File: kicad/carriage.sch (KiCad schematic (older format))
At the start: 44 parts, among them CON10 Stepstick_Left_Connector, CON11 Stepstick_Right_Connector, CON12 Stepstick_Left_Connector, CON13 Stepstick_Right_Connector, CON14 Stepstick_Left_Connector, CON15 Stepstick_Right_Connector, CON9 Carriage, Q1 IRLR2905ZPBF, Q2 IRLR2905ZPBF, Q3 FDC6401N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

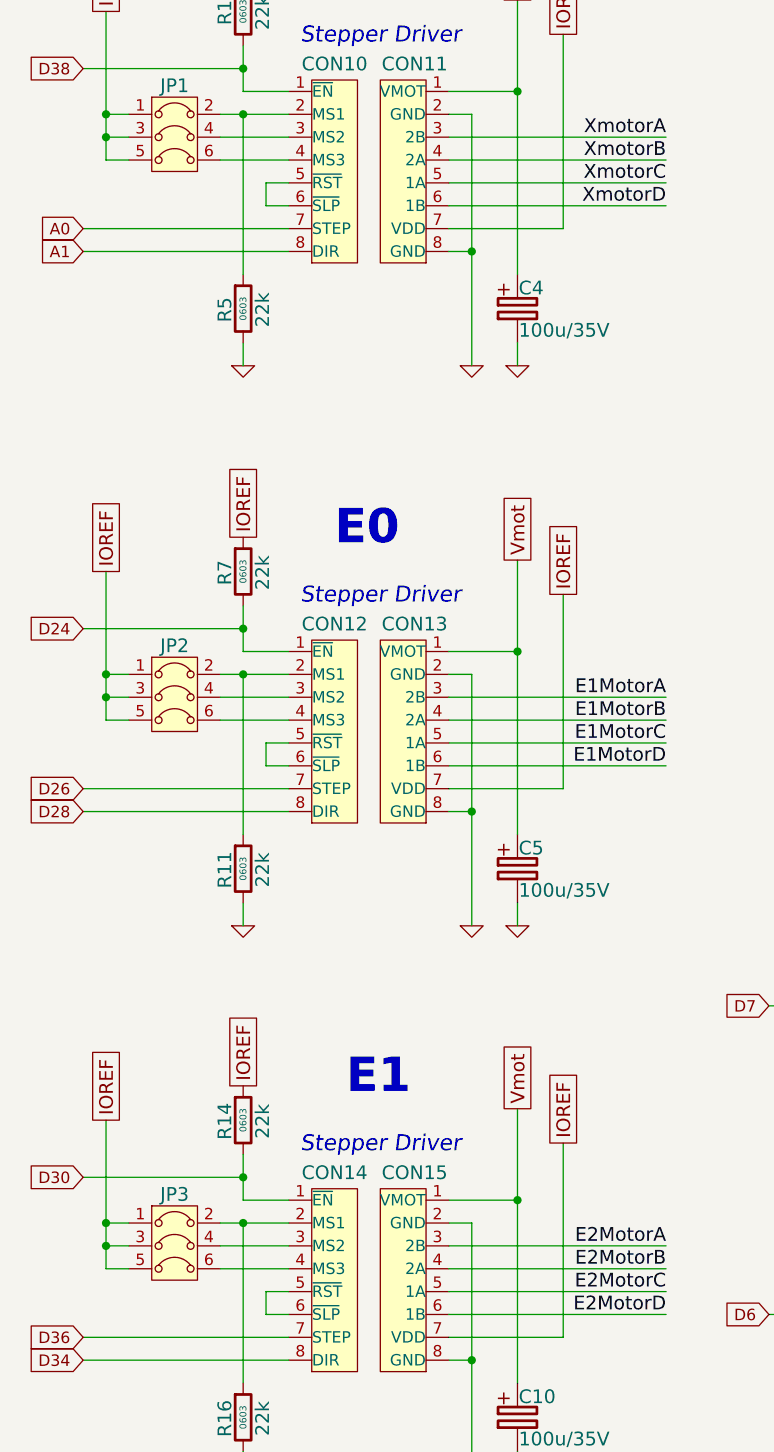
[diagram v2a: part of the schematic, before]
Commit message: Add footprint informations
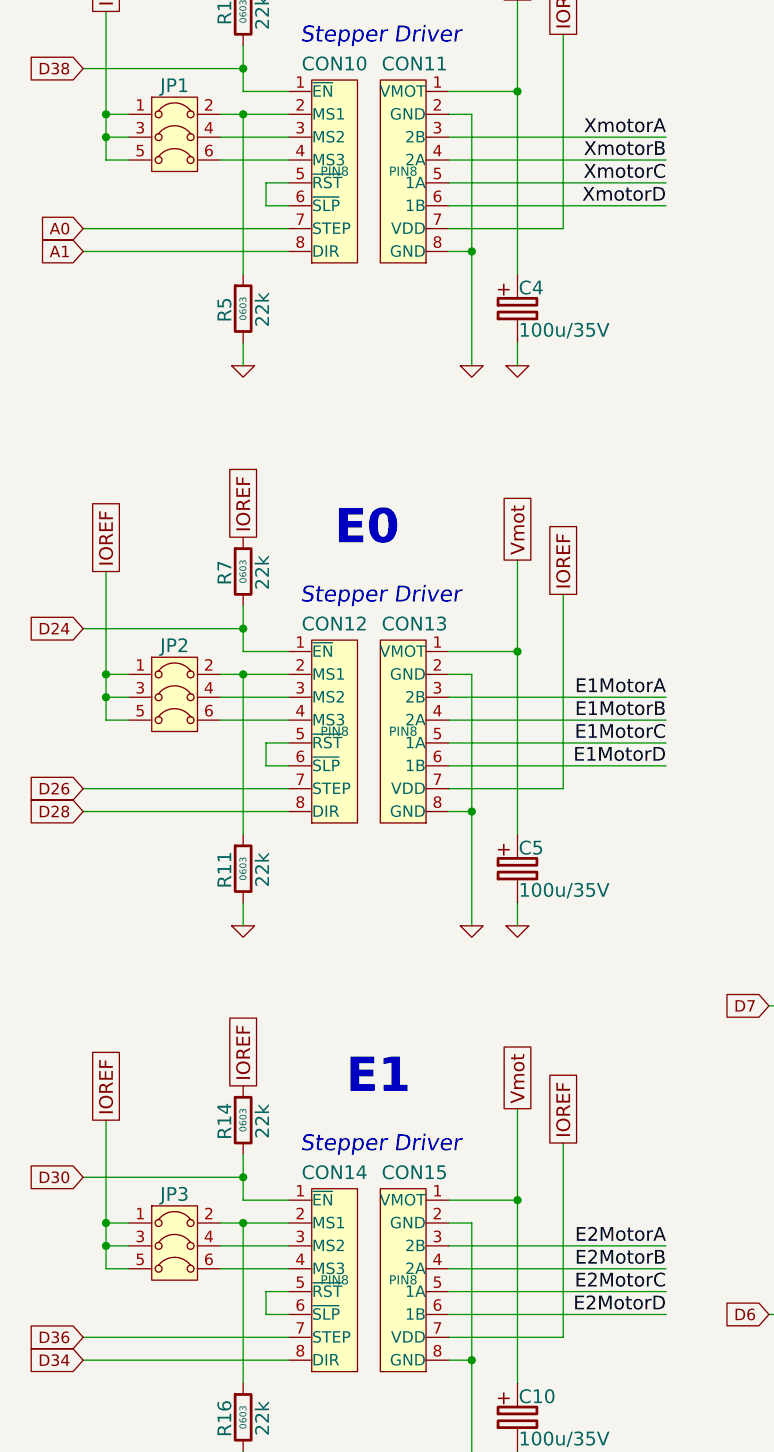
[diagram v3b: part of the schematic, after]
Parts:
- CON10, CON11, CON12, CON13, CON14, CON15: footprint (none) -> PIN8
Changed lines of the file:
@@
 F 0 "CON10" H 2100 2120 60  0000 C CNN
 F 1 "Stepstick_Left_Connector" H 2100 1200 60  0001 C CNN
-F 2 "" H 2100 1650 40  0000 C CNN
+F 2 "PIN8" H 2100 1650 40  0000 C CNN
 F 3 "" H 2100 1650 40  0000 C CNN
 	1    2100 1650
@@
 F 0 "CON11" H 2450 2120 60  0000 C CNN
 F 1 "Stepstick_Right_Connector" H 2450 1200 60  0001 C CNN
-F 2 "" H 2400 1650 40  0000 C CNN
+F 2 "PIN8" H 2400 1650 40  0000 C CNN
 F 3 "" H 2400 1650 40  0000 C CNN
 	1    2450 1650
@@
 F 0 "CON12" H 2100 4570 60  0000 C CNN
 F 1 "Stepstick_Left_Connector" H 2100 3650 60  0001 C CNN
-F 2 "" H 2100 4100 40  0000 C CNN
+F 2 "PIN8" H 2100 4100 40  0000 C CNN
 F 3 "" H 2100 4100 40  0000 C CNN
 	1    2100 4100
@@
 F 0 "CON13" H 2450 4570 60  0000 C CNN
 F 1 "Stepstick_Right_Connector" H 2450 3650 60  0001 C CNN
-F 2 "" H 2400 4100 40  0000 C CNN
+F 2 "PIN8" H 2400 4100 40  0000 C CNN
 F 3 "" H 2400 4100 40  0000 C CNN
 	1    2450 4100
@@
 F 0 "CON14" H 2100 6970 60  0000 C CNN
 F 1 "Stepstick_Left_Connector" H 2100 6050 60  0001 C CNN
-F 2 "" H 2100 6500 40  0000 C CNN
+F 2 "PIN8" H 2100 6500 40  0000 C CNN
 F 3 "" H 2100 6500 40  0000 C CNN
 	1    2100 6500
@@
 F 0 "CON15" H 2450 6970 60  0000 C CNN
 F 1 "Stepstick_Right_Connector" H 2450 6050 60  0001 C CNN
-F 2 "" H 2400 6500 40  0000 C CNN
+F 2 "PIN8" H 2400 6500 40  0000 C CNN
 F 3 "" H 2400 6500 40  0000 C CNN
 	1    2450 6500

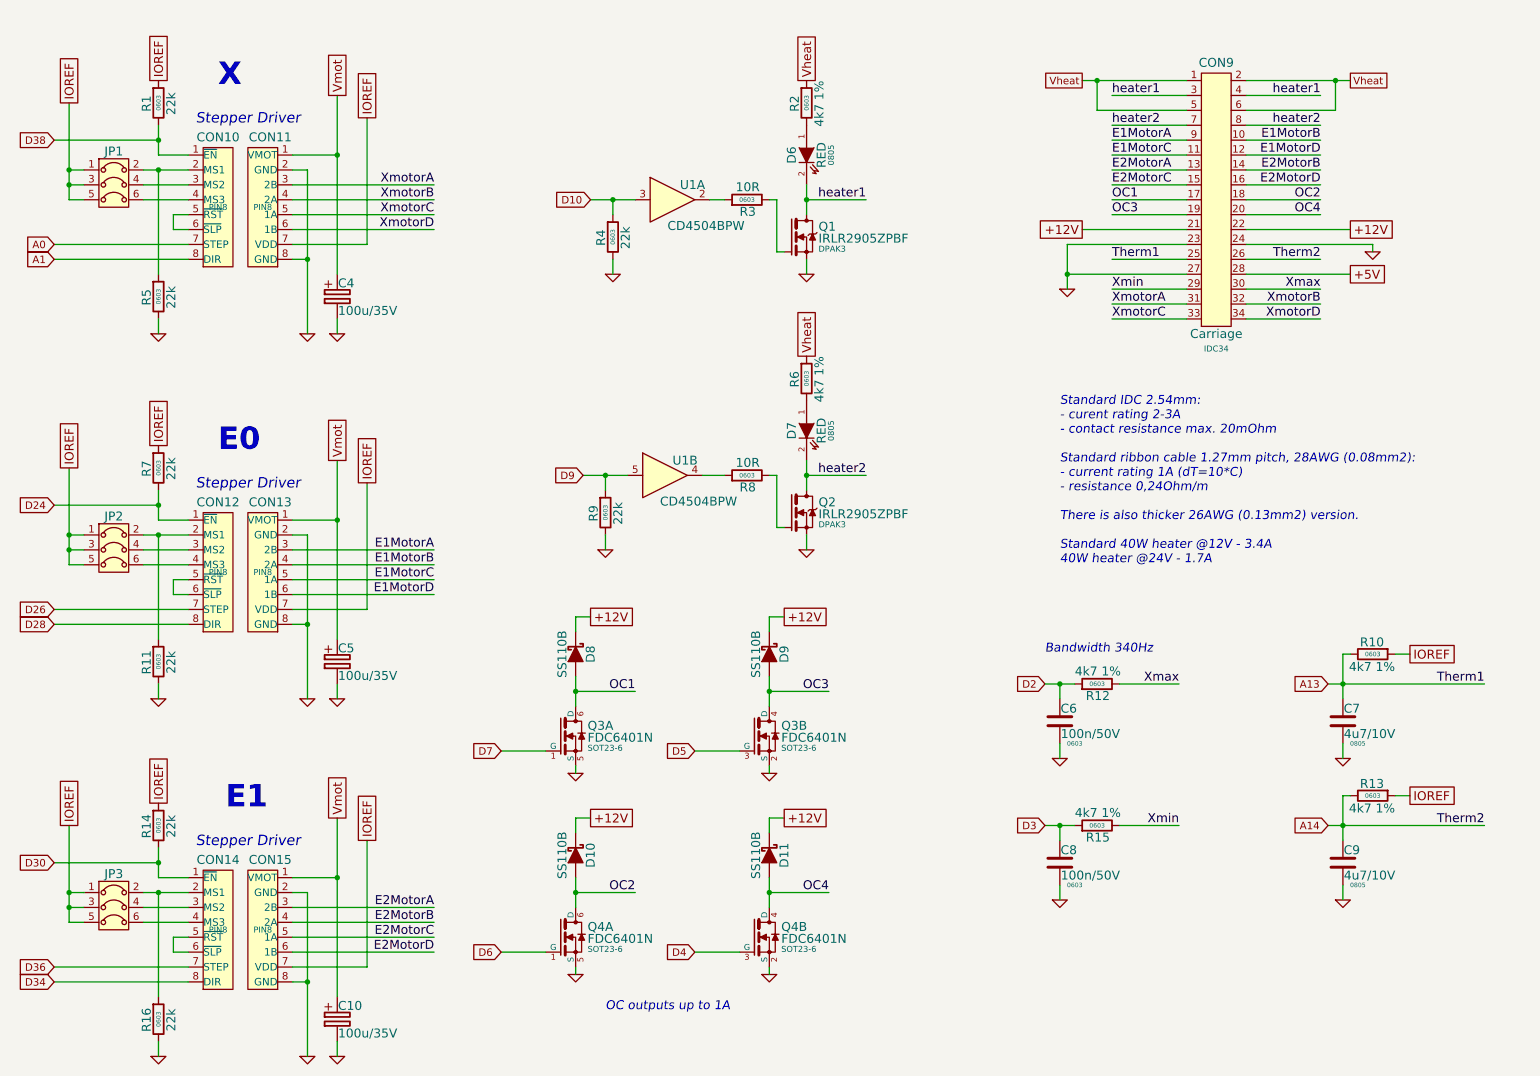
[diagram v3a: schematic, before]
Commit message: Add footprint informations
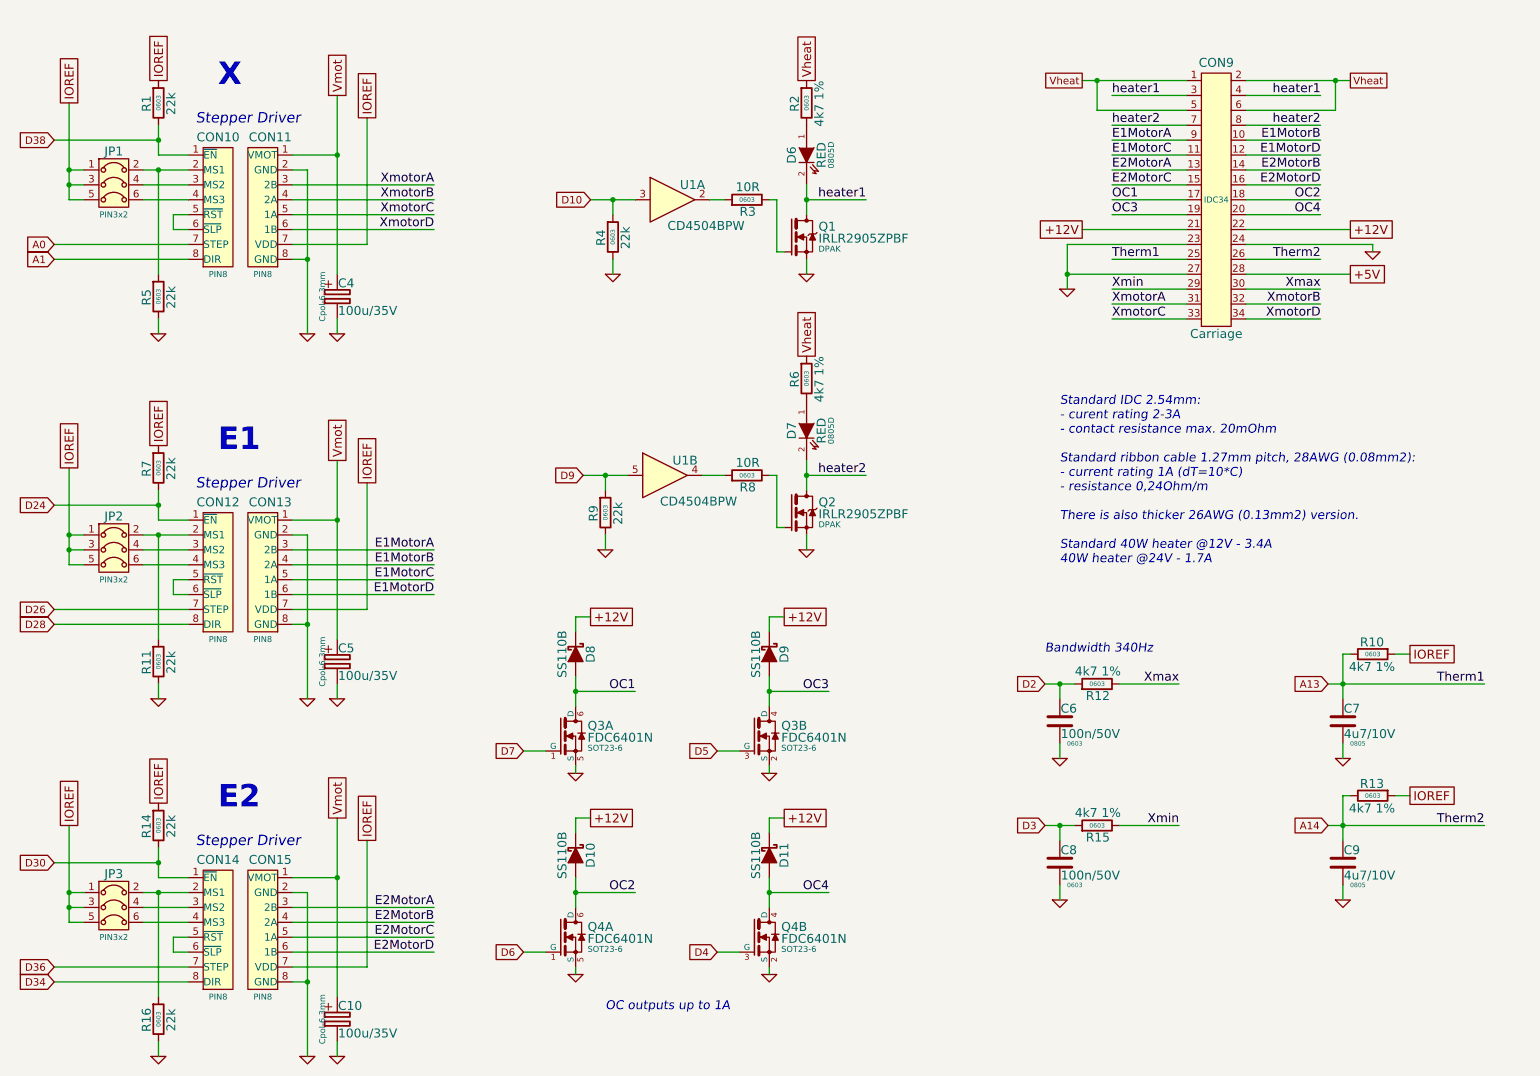
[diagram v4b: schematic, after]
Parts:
- C10, C4, C5: footprint (none) -> Cpol-6.3mm
- D6, D7: footprint 0805 -> 0805D
- JP1, JP2, JP3: footprint (none) -> PIN3x2
- Q1, Q2: footprint DPAK3 -> DPAK
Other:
- note added: "E2"
- note removed: "E0"

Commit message: Add footprint informations
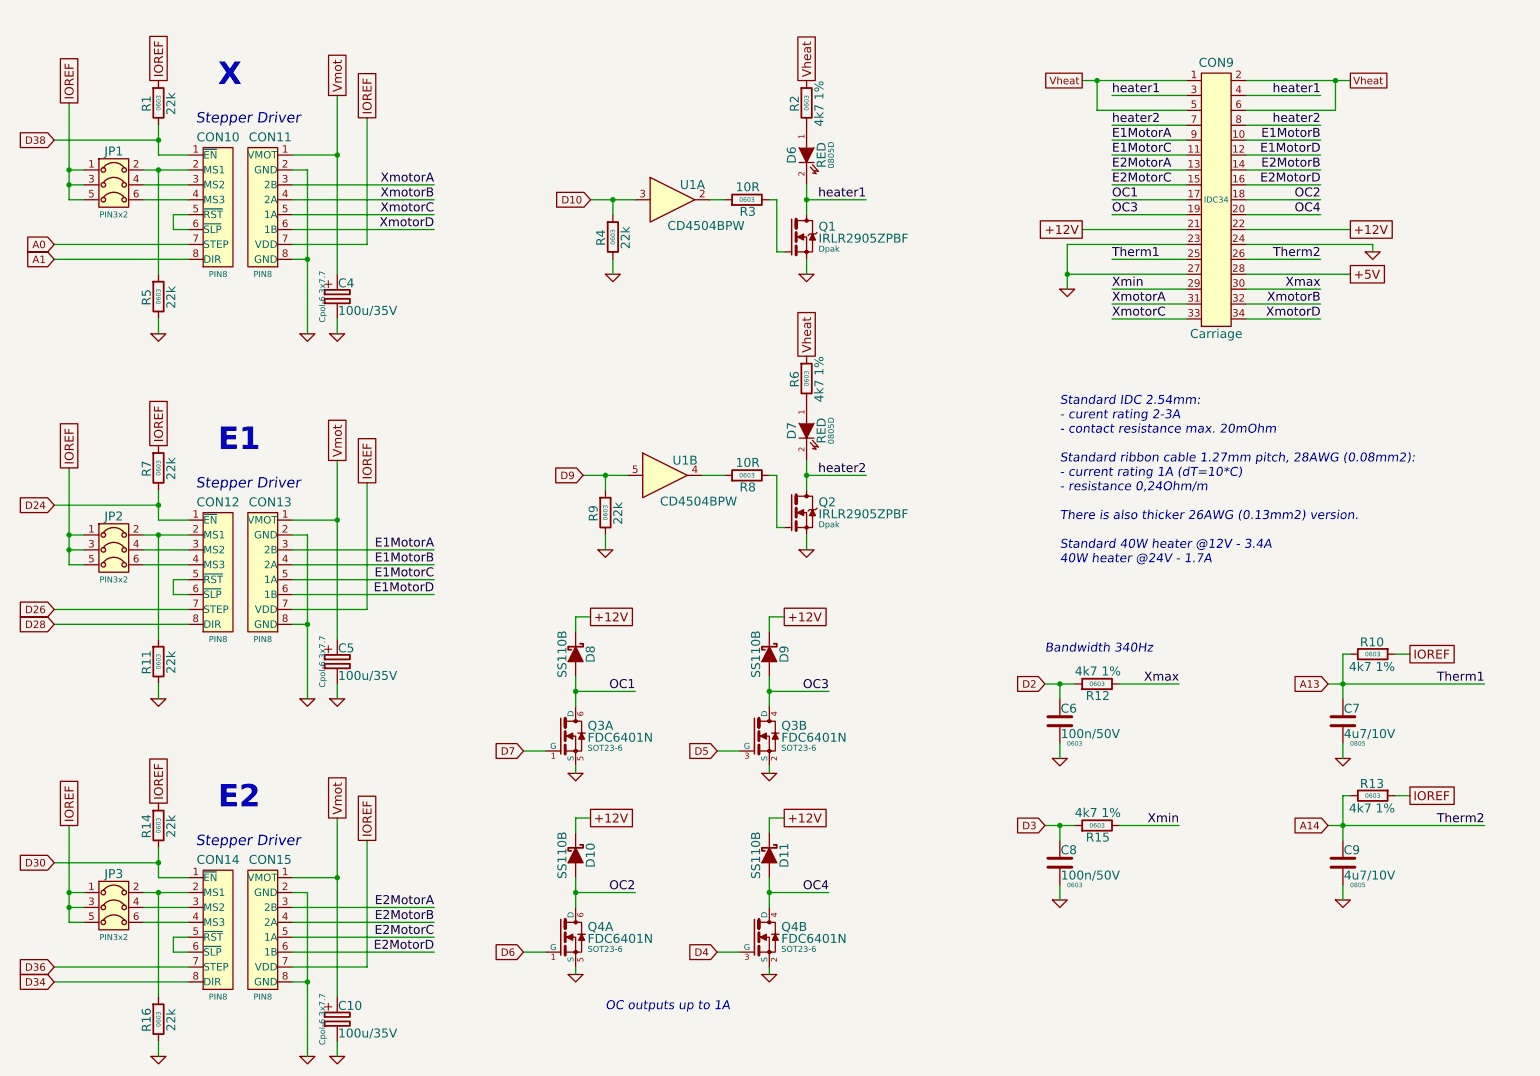
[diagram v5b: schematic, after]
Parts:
- C10, C4, C5: footprint Cpol-6.3mm -> Cpol-6.3x7.7
- Q1, Q2: footprint DPAK -> Dpak

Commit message: Place components
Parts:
- added MECH2: X, symbol stepstickFootprint
- added MECH3: E1, symbol stepstickFootprint
- added MECH4: E2, symbol stepstickFootprint
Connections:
- net IOREF: now also JP1.2, JP1.4, JP1.6, JP2.2, JP2.4, JP2.6, JP3.2, JP3.4, JP3.6; no longer JP1.1, JP1.3, JP1.5, JP2.1, JP2.3, JP2.5, JP3.1, JP3.3, JP3.5
- net at CON10.2 (MS1), R5.1: now also JP1.1; no longer JP1.2
- net at CON10.3 (MS2): now also JP1.3; no longer JP1.4
- net at CON10.4 (MS3): now also JP1.5; no longer JP1.6
- net at CON12.2 (MS1), R11.1: now also JP2.1; no longer JP2.2
- net at CON12.3 (MS2): now also JP2.3; no longer JP2.4
- net at CON12.4 (MS3): now also JP2.5; no longer JP2.6
- net at CON14.2 (MS1), R16.1: now also JP3.1; no longer JP3.2
- net at CON14.3 (MS2): now also JP3.3; no longer JP3.4
- net at CON14.4 (MS3): now also JP3.5; no longer JP3.6
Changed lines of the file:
@@
 F 3 "" H 1250 2100 60  0001 L CNN
 	1    1400 1500
-	1    0    0    -1
+	-1   0    0    -1
 $EndComp
 $Comp
@@
 F 3 "" H 1250 4550 60  0001 L CNN
 	1    1400 3950
-	1    0    0    -1
+	-1   0    0    -1
 $EndComp
 $Comp
@@
 F 3 "" H 1250 6950 60  0001 L CNN
 	1    1400 6350
-	1    0    0    -1
+	-1   0    0    -1
 $EndComp
 $Comp
@@
 Text Notes 1950 5950 0    70   Italic 0
 Stepper Driver
+$Comp
+L stepstickFootprint MECH2
+U 1 1 539C2138
+P 2200 2300
+F 0 "MECH2" H 2200 2300 60  0000 C CNN
+F 1 "X" H 2200 2200 60  0000 C CNN
+F 2 "" H 2100 2300 60  0000 C CNN
+F 3 "" H 2100 2300 60  0000 C CNN
+	1    2200 2300
+	1    0    0    -1
+$EndComp
+$Comp
+L stepstickFootprint MECH3
+U 1 1 539C21AB
+P 2200 4750
+F 0 "MECH3" H 2200 4750 60  0000 C CNN
+F 1 "E1" H 2200 4650 60  0000 C CNN
+F 2 "" H 2100 4750 60  0000 C CNN
+F 3 "" H 2100 4750 60  0000 C CNN
+	1    2200 4750
+	1    0    0    -1
+$EndComp
+$Comp
+L stepstickFootprint MECH4
+U 1 1 539C21C6
+P 2200 7150
+F 0 "MECH4" H 2200 7150 60  0000 C CNN
+F 1 "E2" H 2200 7050 60  0000 C CNN
+F 2 "" H 2100 7150 60  0000 C CNN
+F 3 "" H 2100 7150 60  0000 C CNN
+	1    2200 7150
+	1    0    0    -1
+$EndComp
 $EndSCHEMATC
